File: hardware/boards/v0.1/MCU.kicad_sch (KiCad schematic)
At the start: 38 parts, among them SW24 NRST, SW25 BOOT0, U1 BMDU, U18 STM32H743ZIT6, Y1 7E032768H01, Y4 X322525MOB4SI

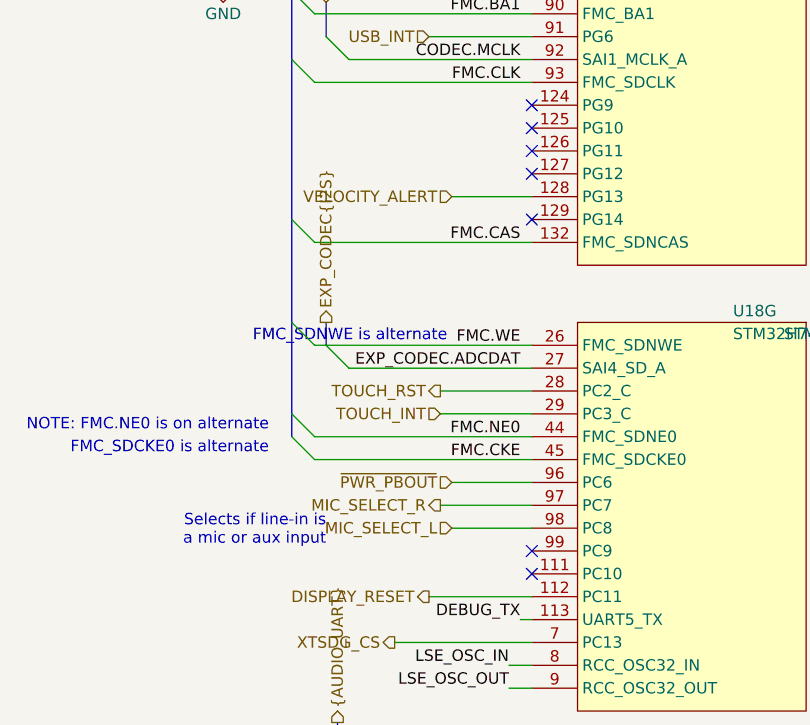
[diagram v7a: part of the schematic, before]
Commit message: feat: add LCD backlight control
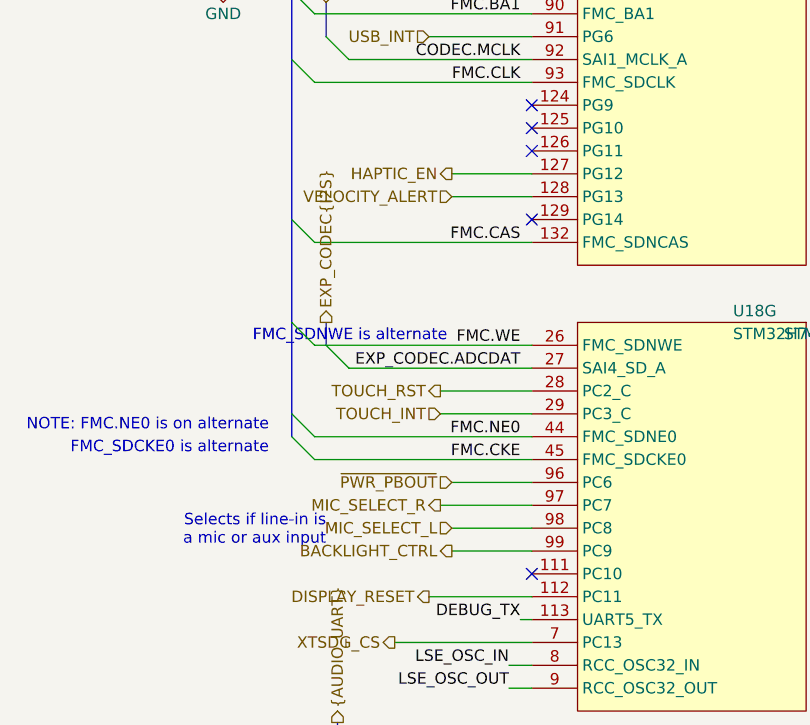
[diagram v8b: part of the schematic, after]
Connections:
- net BACKLIGHT_CTRL: now reaches U18.99 (PC9)
- net HAPTIC_EN: now reaches U18.127 (PG12)
- no-connect marks 12 -> 10
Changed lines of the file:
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@@
 	)
 	(no_connect
-		(at 195.58 55.88)
-	)
-	(no_connect
 		(at 195.58 53.34)
 	)
@@
 	)
 	(no_connect
-		(at 195.58 97.79)
-	)
-	(no_connect
 		(at 195.58 100.33)
 	)
@@
 		)
 	)
+	(wire
+		(pts
+			(xy 186.69 55.88) (xy 195.58 55.88)
+		)
+		(stroke
+			(width 0)
+			(type default)
+		)
+	)
 	(bus
 		(pts
@@
 	(wire
 		(pts
+			(xy 186.69 97.79) (xy 195.58 97.79)
+		)
+		(stroke
+			(width 0)
+			(type default)
+		)
+	)
+	(wire
+		(pts
 			(xy 137.16 137.16) (xy 142.24 137.16)
 		)
@@
 		)
 	)
+	(hierarchical_label "BACKLIGHT_CTRL"
+		(shape output)
+		(at 186.69 97.79 180)
+		(effects
+			(font
+				(size 1.27 1.27)
+			)
+			(justify right)
+		)
+	)
 	(hierarchical_label "MIC_SELECT_R"
 		(shape output)
@@
 		)
 	)
+	(hierarchical_label "HAPTIC_EN"
+		(shape output)
+		(at 186.69 55.88 180)
+		(effects
+			(font
+				(size 1.27 1.27)
+			)
+			(justify right)
+		)
+	)
 	(hierarchical_label "{QSPI}"
 		(shape output)
@@
 			)
 		)
+		(property "Arrow Part Number" ""
+			(at 106.68 68.58 0)
+			(effects
+				(font
+					(size 1.27 1.27)
+				)
+			)
+		)
+		(property "Arrow Price/Stock" ""
+			(at 106.68 68.58 0)
+			(effects
+				(font
+					(size 1.27 1.27)
+				)
+			)
+		)
 		(pin "142"
 		)
@@
 			)
 		)
+		(property "Arrow Part Number" ""
+			(at 213.36 140.97 0)
+			(effects
+				(font
+					(size 1.27 1.27)
+				)
+			)
+		)
+		(property "Arrow Price/Stock" ""
+			(at 213.36 140.97 0)
+			(effects
+				(font
+					(size 1.27 1.27)
+				)
+			)
+		)
 		(pin "142"
 		)
@@
 			)
 		)
+		(property "Arrow Part Number" ""
+			(at 242.57 140.97 0)
+			(effects
+				(font
+					(size 1.27 1.27)
+				)
+			)
+		)
+		(property "Arrow Price/Stock" ""
+			(at 242.57 140.97 0)
+			(effects
+				(font
+					(size 1.27 1.27)
+				)
+			)
+		)
 		(pin "142"
 		)
@@
 			)
 		)
+		(property "Arrow Part Number" ""
+			(at 242.57 44.45 0)
+			(effects
+				(font
+					(size 1.27 1.27)
+				)
+			)
+		)
+		(property "Arrow Price/Stock" ""
+			(at 242.57 44.45 0)
+			(effects
+				(font
+					(size 1.27 1.27)
+				)
+			)
+		)
 		(pin "142"
 			(alternate "FMC_NBL1")
@@
 			)
 		)
+		(property "Arrow Part Number" ""
+			(at 242.57 93.98 0)
+			(effects
+				(font
+					(size 1.27 1.27)
+				)
+			)
+		)
+		(property "Arrow Price/Stock" ""
+			(at 242.57 93.98 0)
+			(effects
+				(font
+					(size 1.27 1.27)
+				)
+			)
+		)
 		(pin "142"
 		)
@@
 	)
 	(symbol
-		(lib_name "STM32H743ZITx_1")
 		(lib_id "pocket_synth:STM32H743ZITx")
 		(at 213.36 93.98 0)
@@
 			)
 		)
+		(property "Arrow Part Number" ""
+			(at 213.36 93.98 0)
+			(effects
+				(font
+					(size 1.27 1.27)
+				)
+			)
+		)
+		(property "Arrow Price/Stock" ""
+			(at 213.36 93.98 0)
+			(effects
+				(font
+					(size 1.27 1.27)
+				)
+			)
+		)
 		(pin "142"
 		)
@@
 	)
 	(symbol
-		(lib_name "STM32H743ZITx_2")
 		(lib_id "pocket_synth:STM32H743ZITx")
 		(at 213.36 44.45 0)
@@
 			)
 		)
+		(property "Arrow Part Number" ""
+			(at 213.36 44.45 0)
+			(effects
+				(font
+					(size 1.27 1.27)
+				)
+			)
+		)
+		(property "Arrow Price/Stock" ""
+			(at 213.36 44.45 0)
+			(effects
+				(font
+					(size 1.27 1.27)
+				)
+			)
+		)
 		(pin "142"
 		)
@@
 			(at 160.02 140.97 0)
 			(effects
+				(font
+					(size 1.27 1.27)
+				)
+			)
+		)
+		(property "Arrow Part Number" ""
+			(at 160.02 140.97 0)
+			(effects
+				(font
+					(size 1.27 1.27)
+				)
+			)
+		)
+		(property "Arrow Price/Stock" ""
+			(at 160.02 140.97 0)
+			(effects
